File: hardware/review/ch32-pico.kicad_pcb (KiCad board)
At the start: 4 copper layers, 21 x 51 mm, 55 parts, among them J1 PICO 40-PIN, J2 GT-USB-7010AW, SW1 RESET, SW2 BOOT, U1 CH32X035C8T6, U4 SY8301ABC

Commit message: Use the GT-USB-7010ASV USB-C receptacle
The AW variant showed no stock at order time. The ASV (C2988369, 117k
reported, 3 A contacts) is the part our land pattern was drawn from, so the
copper is unchanged; the footprint takes the family name, and the 5 A AN
variant is the approved substitute. The symbol, model frame offset, render
model, mechanical check, procurement snapshot, stock table and cost figures
follow: parts are $2.15 per board at 20.
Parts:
- J2: value GT-USB-7010AW -> GT-USB-7010ASV; footprint ch32-pico:USB_C_Receptacle_G-Switch_GT-USB-7010AW -> ch32-pico:USB_C_Receptacle_G-Switch_GT-USB-7010
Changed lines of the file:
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@@
 		(embedded_fonts no)
 	)
-	(footprint "ch32-pico:USB_C_Receptacle_G-Switch_GT-USB-7010AW"
+	(footprint "ch32-pico:USB_C_Receptacle_G-Switch_GT-USB-7010"
 		(layer "F.Cu")
 		(at 10.5 3.375 180)
@@
 			)
 		)
-		(property "Value" "GT-USB-7010AW"
+		(property "Value" "GT-USB-7010ASV"
 			(at 0 5 180)
 			(layer "F.Fab")
@@
 			)
 		)
-		(property "LCSC Part" "C963411"
+		(property "LCSC Part" "C2988369"
 			(at 0 5 180)
 			(layer "F.Fab")

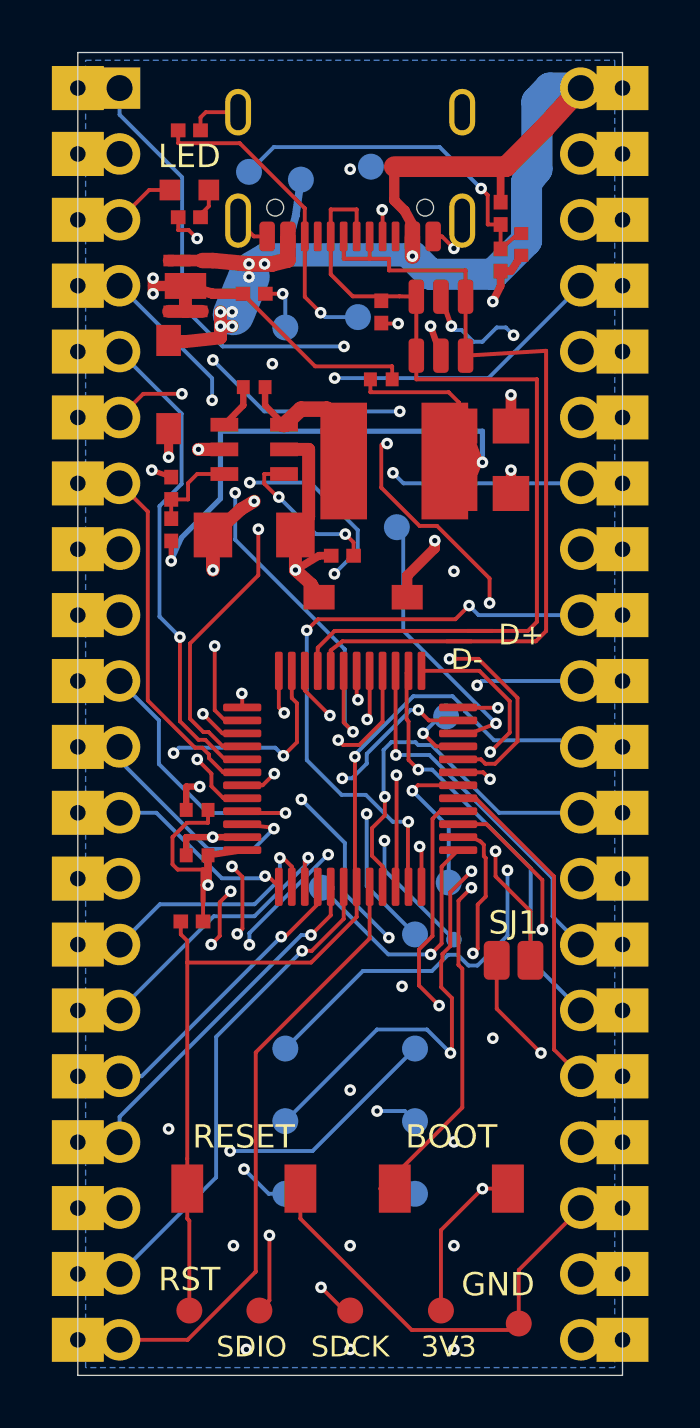
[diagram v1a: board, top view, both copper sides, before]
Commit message: Space the buck output caps off the inductor and reroute
Move C2/C3, C11, D1 and D5 so every fitted courtyard keeps at least 0.2 mm
from its neighbours, and add a courtyard-gap check to placement
verification. Reroute the board, re-plan the ground stitch grid and refresh
the review checkpoint, renders and fabrication outputs.
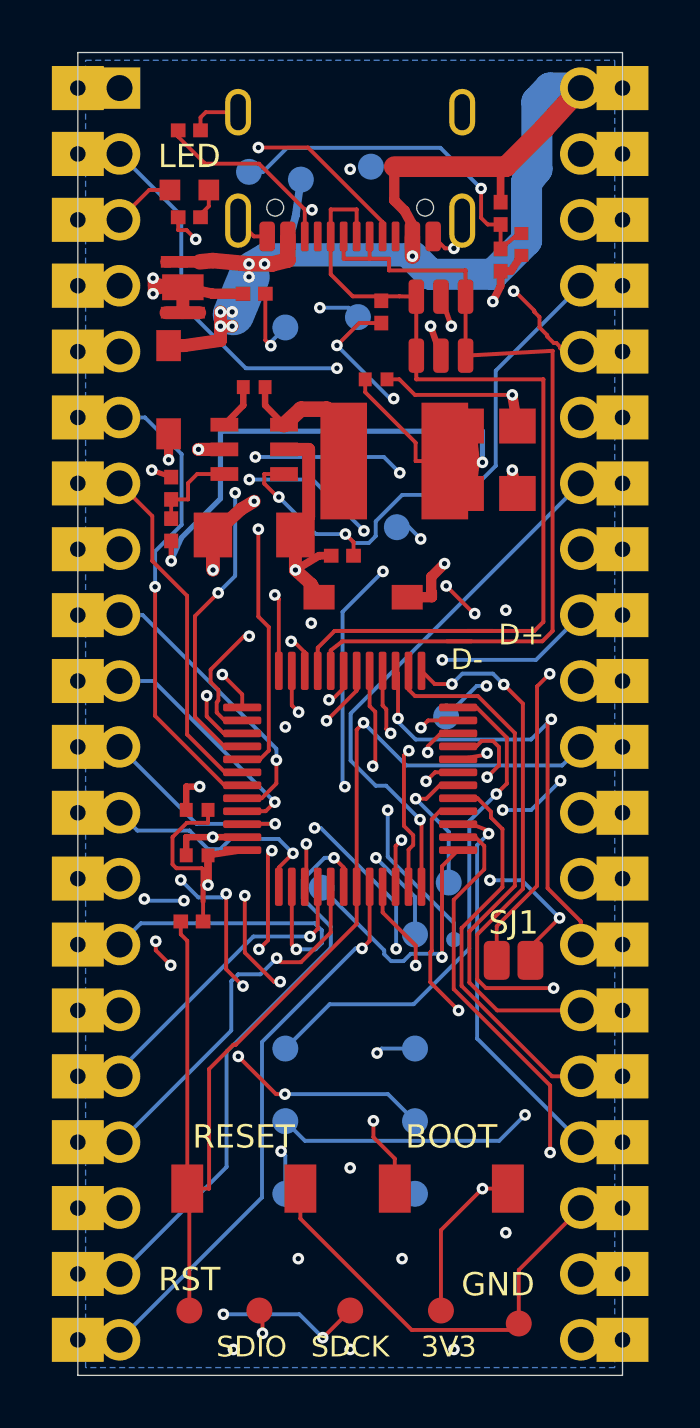
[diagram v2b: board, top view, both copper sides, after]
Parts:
- moved C2 0.25 mm to (15.9, 14.4)
- moved C3 0.25 mm to (15.9, 17.0)
- moved C11 0.20 mm to (11.5, 12.6)
- moved D1 0.20 mm to (3.50, 13.0)
- moved D5 0.11 mm to (4.05, 9.05)
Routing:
- net PA17: track 11.0 -> 33.9 mm
- net PB12: track 33.0 -> 18.4 mm, vias 3 -> 4
- net PB13: track 20.5 -> 33.1 mm, vias 4 -> 5
- net CC2: track 31.4 -> 39.5 mm, vias 2 -> 3
- net PA1: track 23.5 -> 15.8 mm, vias 3 -> 2
- net PB5: track 26.9 -> 34.5 mm, vias 3 -> 4
- net SDCK: track 27.2 -> 34.3 mm, vias 4 -> 5
- net GPIO35: track 29.4 -> 22.3 mm
- net PA21: track 39.2 -> 45.9 mm
- net PA11: track 24.5 -> 18.0 mm, vias 4 -> 1
- net PB1: track 2.72 -> 9.07 mm, vias 1 -> 2
- net SDIO: track 26.9 -> 32.9 mm, vias 4 -> 5
- net CC1: track 31.6 -> 36.4 mm
- net PB6: track 16.2 -> 20.6 mm, vias 1 -> 0
- net PB8: track 28.4 -> 24.5 mm
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
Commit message: Rebuild footprint courtyards and re-space the buck output stage
The EasyEDA-imported footprints drew the package body on the courtyard
layer, so KiCad's courtyard check and the placement gate never saw pad
overlaps; the buck output capacitors actually overlapped the inductor pad.
Draw real courtyards (pads and body plus 0.25 mm, 0.15 mm for 0402) in the
vendoring script, reject any overlap, and re-space the parts the new check
caught: output caps turned vertical beside the inductor with a locked feed
and dedicated ground vias, input cap, sense divider, feedback resistors,
input diode, LED and its resistor.

Lock an inner-layer link from the 3.3 V trunk to the ESD diode supply so the
router no longer adds a staircase of surface stubs beside header pin 36.
Move the VSNS probe pad under the inductor where its label fits, step the
CC, PB2, PB3 and ground labels off their neighbouring pads, and give the
expansion labels more clearance. Reroute, re-plan the ground stitch grid and
refresh the review checkpoint, renders and fabrication outputs.
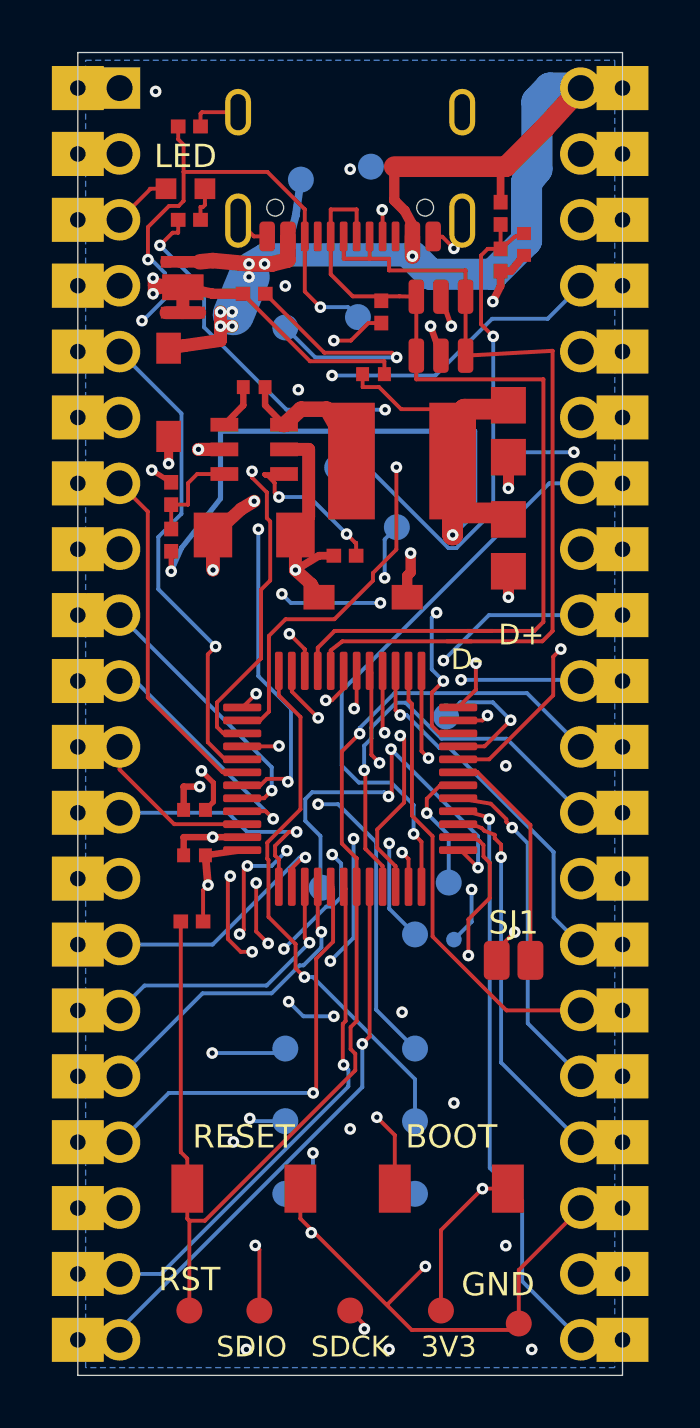
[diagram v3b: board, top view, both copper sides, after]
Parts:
- moved TP17 11.9 mm to (10.0, 16.0)
- moved C3 2.10 mm to (16.6, 19.0), turned to -90 degrees
- moved C2 0.68 mm to (16.6, 14.6), turned to -90 degrees
- moved R13 0.40 mm to (3.60, 18.8)
- moved L1 0.30 mm to (12.5, 15.8)
- moved C11 0.22 mm to (11.4, 12.4)
- moved R14 0.20 mm to (3.60, 17.0)
- moved D3 0.16 mm to (4.15, 5.25)
- moved R4 0.15 mm to (4.30, 2.85)
- moved R15 0.10 mm to (10.3, 19.4)
- moved R11 0.10 mm to (4.30, 6.45)
- moved C6 0.10 mm to (4.50, 30.9)
- moved C7 0.10 mm to (4.50, 29.2)
- moved D1 0.10 mm to (3.50, 13.1)
- moved C9 0.10 mm to (17.2, 7.40)
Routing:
- net PA17: track 33.9 -> 10.6 mm
- net PB4: track 19.8 -> 32.9 mm, vias 1 -> 4
- net PB13: track 33.1 -> 20.8 mm, vias 5 -> 1
- net PB5: track 34.5 -> 26.6 mm, vias 4 -> 5
- net SDCK: track 34.3 -> 28.0 mm, vias 5 -> 4
- net 3V3_OUT: track 89.7 -> 95.8 mm
- net PA3: track 10.5 -> 16.0 mm, vias 1 -> 3
- net GND: track 54.6 -> 59.3 mm, vias 24 -> 28
- net PB7: track 17.8 -> 13.9 mm, vias 2 -> 1
- net PB10: track 33.4 -> 29.7 mm, vias 3 -> 1
- net PB1: track 9.07 -> 5.44 mm, vias 2 -> 1
- net SDIO: track 32.9 -> 29.7 mm, vias 5 -> 4
- net PB6: track 20.6 -> 17.5 mm
- net PA23: track 14.0 -> 16.8 mm
- net PC7: track 11.6 -> 8.85 mm, vias 3 -> 0
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
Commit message: Align the corner header legends with their rows
Put the names for pins 1, 20, 21 and 40 beside their pads like every other
row and place the pin numbers just inward of them, past the USB shell stakes
at the top. The two names beside the stakes use condensed 0.7 mm wide type
to keep 0.3 mm from the pads. Drop the bracket leaders that reached around
the stakes.
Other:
- board text added: "1"
- board text added: "20"
- board text added: "21"
- board text added: "40"
- board text added: "PA22"
- board text added: "PA6"
- board text added: "PB10"
- board text removed: "1 PB10"
- board text removed: "20 PA22"
- board text removed: "21 PA6"
- board text removed: "40 VBUS"
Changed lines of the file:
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@@
-	)
-	(gr_line
-		(start 3.4 0.8)
-		(end 2.85 1.37)
-		(stroke
-			(width 0.15)
-			(type solid)
-		)
-		(layer "B.SilkS")
-	)
-	(gr_line
-		(start 7.1 0.8)
-		(end 3.4 0.8)
-		(stroke
-			(width 0.15)
-			(type solid)
-		)
-		(layer "B.SilkS")
-	)
-	(gr_line
-		(start 7.1 1.37)
-		(end 7.1 0.8)
-		(stroke
-			(width 0.15)
-			(type solid)
-		)
-		(layer "B.SilkS")
 	)
 	(gr_line
@@
 	)
 	(gr_line
-		(start 13.9 0.8)
-		(end 17.73 0.8)
-		(stroke
-			(width 0.15)
-			(type solid)
-		)
-		(layer "B.SilkS")
-	)
-	(gr_line
-		(start 13.9 3.15)
-		(end 13.9 0.8)
-		(stroke
-			(width 0.15)
-			(type solid)
-		)
-		(layer "B.SilkS")
-	)
-	(gr_line
 		(start 14 47.5)
 		(end 14.3 47.8)
@@
 	)
 	(gr_line
-		(start 17.73 0.8)
-		(end 18.3 1.37)
-		(stroke
-			(width 0.15)
-			(type solid)
-		)
-		(layer "B.SilkS")
-	)
-	(gr_line
 		(start 0 0)
 		(end 21 0)
@@
 		)
 	)
+	(gr_text "PB10"
+		(at 4.05 1.37 0)
+		(layer "B.SilkS")
+		(effects
+			(font
+				(size 0.8 0.7)
+				(thickness 0.15)
+			)
+			(justify mirror)
+		)
+	)
+	(gr_text "VBUS"
+		(at 16.95 1.37 0)
+		(layer "B.SilkS")
+		(effects
+			(font
+				(size 0.8 0.7)
+				(thickness 0.15)
+			)
+			(justify mirror)
+		)
+	)
 	(gr_text "GND"
 		(at 4.3 6.45 0)
@@
 		)
 	)
-	(gr_text "20 PA22"
-		(at 5.2 49.63 0)
+	(gr_text "PA22"
+		(at 4.4 49.63 0)
+		(layer "B.SilkS")
+		(effects
+			(font
+				(size 0.8 0.8)
+				(thickness 0.15)
+			)
+			(justify mirror)
+		)
+	)
+	(gr_text "20"
+		(at 7 49.63 0)
+		(layer "B.SilkS")
+		(effects
+			(font
+				(size 0.8 0.8)
+				(thickness 0.15)
+			)
+			(justify mirror)
+		)
+	)
+	(gr_text "1"
+		(at 7.25 1.37 0)
 		(layer "B.SilkS")
 		(effects
@@
 		)
 	)
-	(gr_text "1 PB10"
-		(at 10 1.37 0)
-		(layer "B.SilkS")
-		(effects
-			(font
-				(size 0.8 0.8)
-				(thickness 0.15)
-			)
-			(justify mirror)
-		)
-	)
 	(gr_text "VSNS"
 		(at 10 17.2 0)
@@
 		)
 	)
-	(gr_text "40 VBUS"
-		(at 10.5 3.15 0)
-		(layer "B.SilkS")
-		(effects
-			(font
-				(size 0.8 0.8)
-				(thickness 0.15)
-			)
-			(justify mirror)
-		)
-	)
 	(gr_text "VBUS 5-20V"
 		(at 10.5 13 0)
@@
 		)
 	)
+	(gr_text "40"
+		(at 13.4 1.37 0)
+		(layer "B.SilkS")
+		(effects
+			(font
+				(size 0.8 0.8)
+				(thickness 0.15)
+			)
+			(justify mirror)
+		)
+	)
 	(gr_text "PC6"
 		(at 14.1 30.9 0)
@@
 		)
 	)
+	(gr_text "21"
+		(at 14.35 49.63 0)
+		(layer "B.SilkS")
+		(effects
+			(font
+				(size 0.8 0.8)
+				(thickness 0.15)
+			)
+			(justify mirror)
+		)
+	)
 	(gr_text "PB3"
 		(at 14.85 33.2 0)
@@
 		)
 	)
-	(gr_text "21 PA6"
-		(at 15.8 49.63 0)
-		(layer "B.SilkS")
-		(effects
-			(font
-				(size 0.8 0.8)
-				(thickness 0.15)
-			)
-			(justify mirror)
-		)
-	)
 	(gr_text "VSYS"
 		(at 16.6 3.91 0)
@@
 		(layer "B.SilkS")
 		(effects
+			(font
+				(size 0.8 0.8)
+				(thickness 0.15)
+			)
+			(justify mirror)
+		)
+	)
+	(gr_text "PA6"
+		(at 16.6 49.63 0)
+		(layer "B.SilkS")
+		(effects
